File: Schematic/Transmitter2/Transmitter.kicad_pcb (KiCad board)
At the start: 2 copper layers, 25 x 94 mm, 50 parts, among them J1 Conn_01x06, J2 Antenna, J3 Conn_01x01, Q1 MMBT3904, Q2 MMBT3904, Q3 MMBT3904, U1 SN74HCU04N, U2 MH-M18, U3 SN74LS74AN, U4 LF351D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

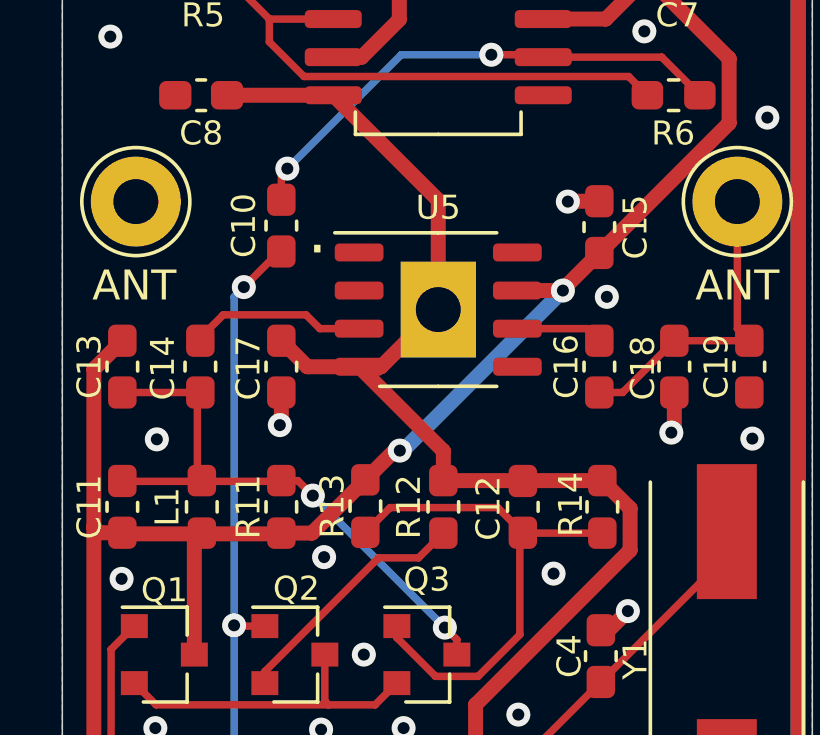
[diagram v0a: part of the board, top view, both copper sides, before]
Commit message: Added missing resistor: R15
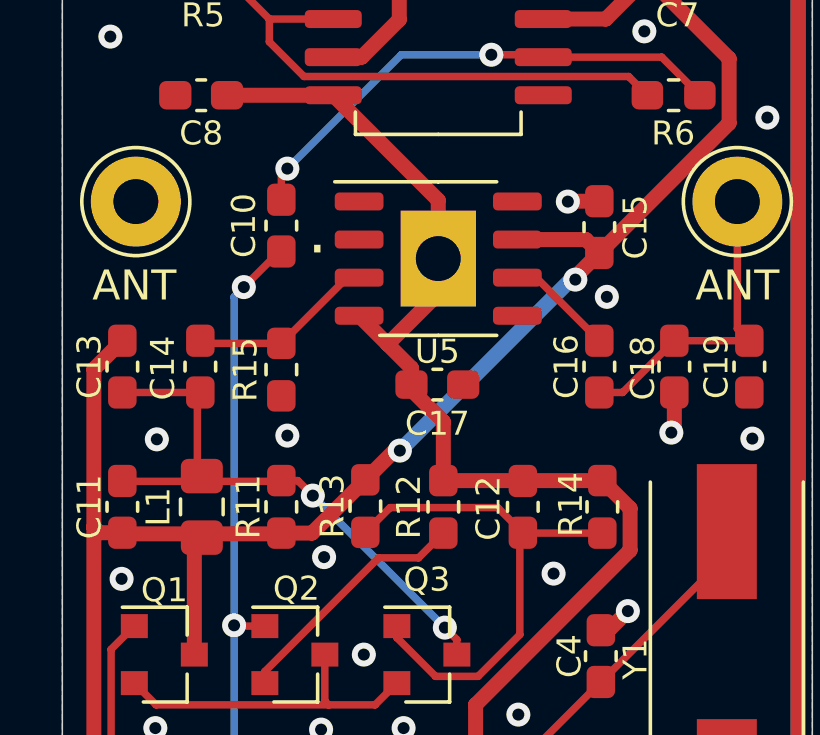
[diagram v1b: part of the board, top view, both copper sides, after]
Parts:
- added R15: 10kΩ, Resistor_SMD:R_0603_1608Metric_Pad1.05x0.95mm_HandSolder, F.Cu at (137.8, 93.6)
- C11: value * -> 390pF
- C13: value * -> 150pF
- L1: value * -> 47µH; footprint Inductor_SMD:L_0603_1608Metric_Pad1.05x0.95mm_HandSolder -> Inductor_SMD:L_0805_2012Metric_Pad1.15x1.40mm_HandSolder
- moved C17 5.23 mm to (143.0, 94.1), turned to 180 degrees
- moved U5 1.70 mm to (143.0, 89.9)
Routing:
- net -12V: track 63.8 -> 61.2 mm
- net +12V: track 80.4 -> 81.9 mm
- net GND: track 12.3 -> 11.2 mm
- net Net-(C16-Pad2): track 2.90 -> 3.60 mm
